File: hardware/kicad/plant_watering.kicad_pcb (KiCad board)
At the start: 2 copper layers, 143 x 112 mm, 52 parts, among them J1 USB-C panel cable (PH2.0 6P), J10 Pump2_12V, J11 Pump3_12V, J12 Pump4_12V, J13 Pump5_12V, J14 Pump6_12V, J15 Float switch (water level), J2 UI MODULE, J3 Sensor1 (GND,VCC,DIS,OUT), J4 Sensor2 (GND,VCC,DIS,OUT), J5 Sensor3 (GND,VCC,DIS,OUT), J6 Sensor4 (GND,VCC,DIS,OUT), J7 Sensor5 (GND,VCC,DIS,OUT), J8 Sensor6 (GND,VCC,DIS,OUT), J9 Pump1_12V, Q1 IRLZ44N, Q2 IRLZ44N, Q3 IRLZ44N, Q4 IRLZ44N, Q5 IRLZ44N, Q6 IRLZ44N, U1 YD-ESP32-23

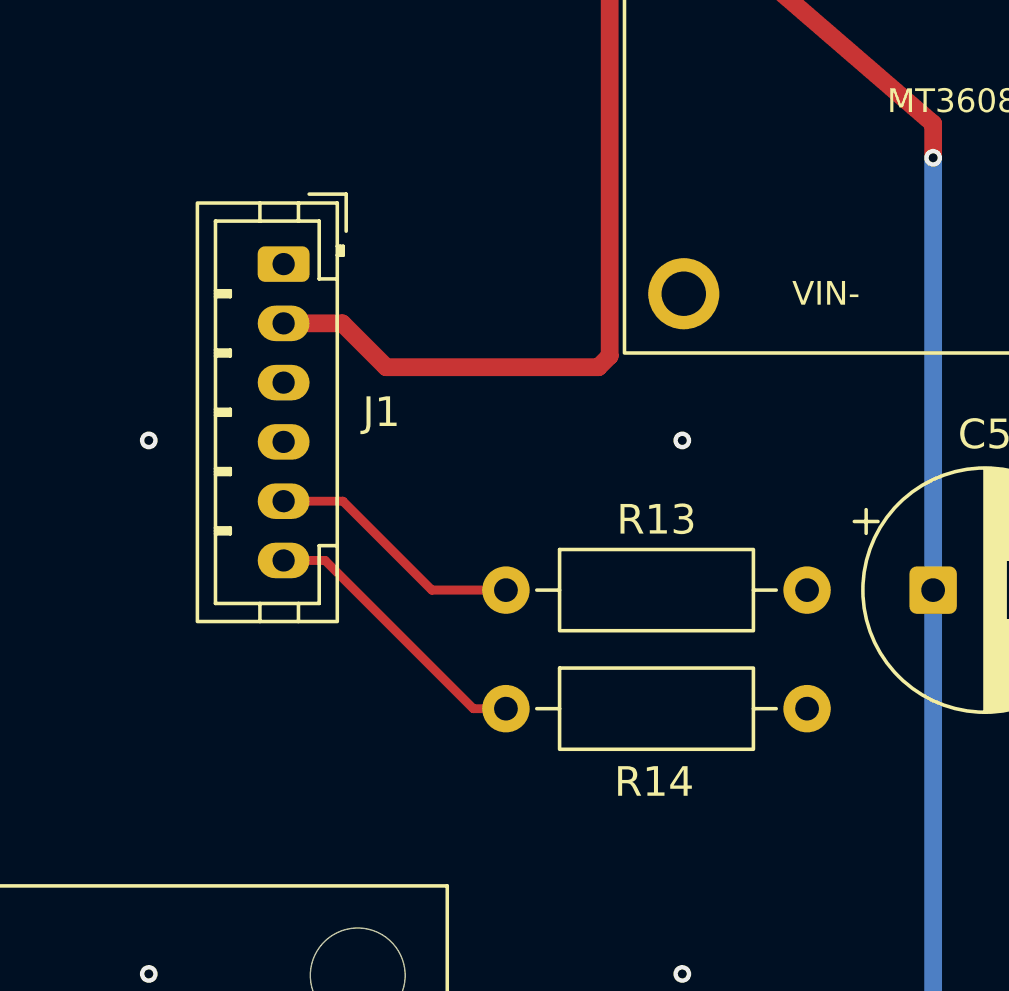
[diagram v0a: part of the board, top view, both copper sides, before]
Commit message: Simplify USB-C power input to a 2-pin V+/V- connector
J1 becomes a JST-XH 2-pin header (1 GND, 2 +5V) for a 2-wire panel
USB-C socket. Drop the CC pull-downs R13/R14 and the CC1/CC2 nets; the
socket must provide its own 5.1k CC resistors for C-to-C chargers.
Update BOM, README and the 3D view image.

Co-Authored-By: Claude Opus 5.5 <noreply@anthropic.com>
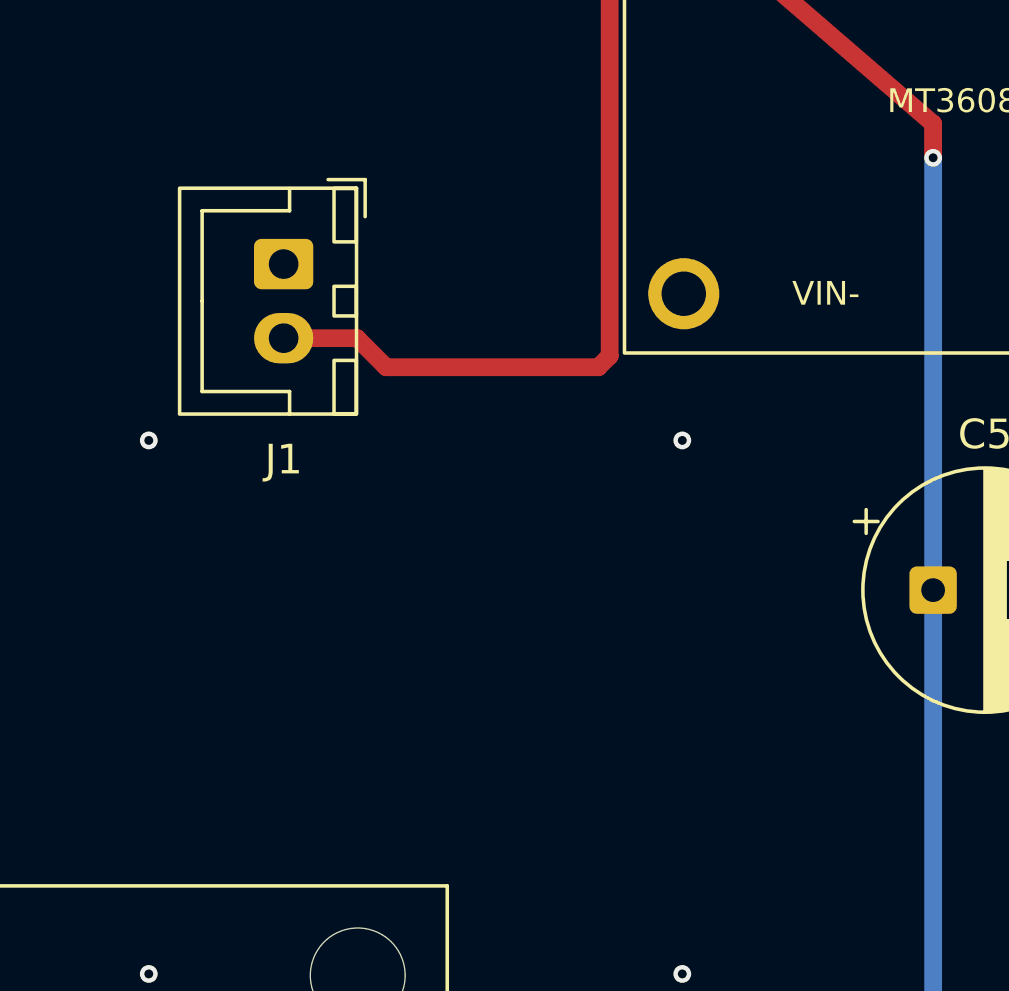
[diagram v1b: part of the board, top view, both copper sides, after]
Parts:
- removed R13, R14: 5.1k, Resistor_THT:R_Axial_DIN0207_L6.3mm_D2.5mm_P10.16mm_Horizontal
- J1: value USB-C panel cable (PH2.0 6P) -> USB-C panel socket (V+/V-); footprint Connector_JST:JST_PH_B6B-PH-K_1x06_P2.00mm_Vertical -> Connector_JST:JST_XH_B2B-XH-A_1x02_P2.50mm_Vertical
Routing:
- net CC2: track 9.57 -> 0.00 mm
- net CC1: track 8.74 -> 0.00 mm

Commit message: Add board title and goat logo to silkscreen; drop prototypy.com export
- Top-left silkscreen: goat logo (source in hardware/kicad/goat_logo.svg)
  and "Another watering system v0.1"
- export_fab.py now writes only the standard Gerber zip; removed the
  prototypy.com zip, their KiCad guide PDF and the related docs
- Regenerated plant_watering-gerbers.zip

Co-Authored-By: Claude Opus 5.5 <noreply@anthropic.com>
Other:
- board text added: "Another watering system v0.1"
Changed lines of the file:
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@@
 		)
+	)
+	(gr_poly
+		(pts
+			(xy 36.351239 55.749031) (xy 36.816115 55.842007) (xy 36.53719 56.771759) (xy 36.351239 55.749031)
+		)
+		(stroke
+			(width 0)
+			(type solid)
+		)
+		(fill yes)
+		(layer "F.SilkS")
+	)
+	(gr_poly
+		(pts
+			(xy 30.493802 56.585809) (xy 29.75 55.656056) (xy 30.028925 55.563081) (xy 30.865702 56.306883) (xy 30.493802 56.585809)
+		)
+		(stroke
+			(width 0)
+			(type solid)
+		)
+		(fill yes)
+		(layer "F.SilkS")
+	)
+	(gr_poly
+		(pts
+			(xy 34.119834 56.399858) (xy 35.328513 54.726304) (xy 36.072314 55.098205) (xy 35.142562 57.32961)
+			(xy 34.119834 56.399858)
+		)
+		(stroke
+			(width 0)
+			(type solid)
+		)
+		(fill yes)
+		(layer "F.SilkS")
+	)
+	(gr_poly
+		(pts
+			(xy 35.421487 55.00523) (xy 34.398761 55.19118) (xy 34.58471 55.470106) (xy 35.514463 55.284155)
+			(xy 35.421487 55.00523)
+		)
+		(stroke
+			(width 0)
+			(type solid)
+		)
+		(fill yes)
+		(layer "F.SilkS")
+	)
+	(gr_poly
+		(pts
+			(xy 30.772728 57.980437) (xy 31.237603 57.980437) (xy 31.144628 60.025891) (xy 31.330579 60.304817)
+			(xy 30.772728 60.304817) (xy 30.772728 60.025891) (xy 30.772728 57.980437)
+		)
+		(stroke
+			(width 0)
+			(type solid)
+		)
+		(fill yes)
+		(layer "F.SilkS")
+	)
+	(gr_poly
+		(pts
+			(xy 31.516529 57.980437) (xy 31.981405 57.980437) (xy 31.88843 60.025891) (xy 32.07438 60.304817)
+			(xy 31.516529 60.304817) (xy 31.516529 60.025891) (xy 31.516529 57.980437)
+		)
+		(stroke
+			(width 0)
+			(type solid)
+		)
+		(fill yes)
+		(layer "F.SilkS")
+	)
+	(gr_poly
+		(pts
+			(xy 33.840909 57.980437) (xy 34.305785 57.980437) (xy 34.21281 60.025891) (xy 34.398761 60.304817)
+			(xy 33.840909 60.304817) (xy 33.840909 60.025891) (xy 33.840909 57.980437)
+		)
+		(stroke
+			(width 0)
+			(type solid)
+		)
+		(fill yes)
+		(layer "F.SilkS")
+	)
+	(gr_poly
+		(pts
+			(xy 34.58471 57.887462) (xy 35.049587 57.701511) (xy 34.956612 60.025891) (xy 35.142562 60.304817)
+			(xy 34.58471 60.304817) (xy 34.58471 60.025891) (xy 34.58471 57.887462)
+		)
+		(stroke
+			(width 0)
+			(type solid)
+		)
+		(fill yes)
+		(layer "F.SilkS")
+	)
+	(gr_poly
+		(pts
+			(xy 35.607438 54.540354) (xy 35.51188 54.392497) (xy 35.411157 54.258846) (xy 35.305268 54.139399)
+			(xy 35.194215 54.034155) (xy 35.077996 53.943118) (xy 34.956612 53.866284) (xy 34.830062 53.803655)
+			(xy 34.698347 53.75523) (xy 34.561467 53.72101) (xy 34.419421 53.700995) (xy 34.27221 53.695184)
+			(xy 34.119834 53.703577) (xy 34.061725 53.719719) (xy 34.011364 53.737152) (xy 33.96875 53.755875)
+			(xy 33.933885 53.775891) (xy 33.906767 53.797198) (xy 33.887397 53.819796) (xy 33.875775 53.843686)
+			(xy 33.871901 53.868867) (xy 33.875775 53.895339) (xy 33.887397 53.923102) (xy 33.906767 53.952156)
+			(xy 33.933885 53.982503) (xy 34.070764 53.973464) (xy 34.202479 53.977337) (xy 34.329029 53.994124)
+			(xy 34.450413 54.023825) (xy 34.566632 54.066438) (xy 34.677686 54.121965) (xy 34.783575 54.190405)
+			(xy 34.884298 54.271759) (xy 34.979855 54.366026) (xy 35.070248 54.473205) (xy 35.155475 54.593298)
+			(xy 35.235537 54.726304) (xy 35.607438 54.540354)
+		)
+		(stroke
+			(width 0)
+			(type solid)
+		)
+		(fill yes)
+		(layer "F.SilkS")
+	)
+	(gr_poly
+		(pts
+			(xy 35.328513 54.633329) (xy 35.405991 54.575866) (xy 35.483471 54.52744) (xy 35.560951 54.488055)
+			(xy 35.63843 54.45771) (xy 35.715909 54.436403) (xy 35.793388 54.424135) (xy 35.870868 54.420906)
+			(xy 35.948347 54.426718) (xy 36.025827 54.441568) (xy 36.103306 54.465458) (xy 36.180785 54.498386)
+			(xy 36.258264 54.540354) (xy 37.188017 55.377131) (xy 37.215135 55.437823) (xy 37.234504 55.495933)
+			(xy 37.246126 55.55146) (xy 37.25 55.604403) (xy 37.246126 55.654765) (xy 37.234504 55.702544) (xy 37.215135 55.747741)
+			(xy 37.188017 55.790354) (xy 37.153151 55.830385) (xy 37.110537 55.867833) (xy 37.060175 55.902699)
+			(xy 37.002066 55.934982) (xy 36.351239 55.842007) (xy 36.244705 55.809078) (xy 36.142045 55.772276)
+			(xy 36.04326 55.731599) (xy 35.948347 55.687048) (xy 35.857309 55.638624) (xy 35.770145 55.586325)
+			(xy 35.686854 55.530153) (xy 35.607438 55.470106) (xy 35.531896 55.406186) (xy 35.460228 55.338391)
+			(xy 35.392433 55.266723) (xy 35.328513 55.19118) (xy 35.328513 54.633329)
+		)
+		(stroke
+			(width 0)
+			(type solid)
+		)
+		(fill yes)
+		(layer "F.SilkS")
+	)
+	(gr_poly
+		(pts
+			(xy 30.400827 56.678784) (xy 30.438275 56.590328) (xy 30.488636 56.510912) (xy 30.551911 56.440534)
+			(xy 30.628099 56.379197) (xy 30.717201 56.326899) (xy 30.819215 56.283639) (xy 30.934143 56.249419)
+			(xy 31.061984 56.224238) (xy 31.202737 56.208097) (xy 31.356405 56.200995) (xy 31.522986 56.202931)
+			(xy 31.70248 56.213907) (xy 34.119834 56.213907) (xy 34.268982 56.233923) (xy 34.406509 56.262978)
+			(xy 34.532412 56.301072) (xy 34.646694 56.348205) (xy 34.749354 56.404378) (xy 34.840393 56.469589)
+			(xy 34.919809 56.54384) (xy 34.987603 56.627131) (xy 35.043776 56.719461) (xy 35.088327 56.820829)
+			(xy 35.121255 56.931237) (xy 35.142562 57.050684) (xy 35.152247 57.201124) (xy 35.15031 57.342524)
+			(xy 35.136751 57.474884) (xy 35.11157 57.598205) (xy 35.074768 57.712487) (xy 35.026343 57.81773)
+			(xy 34.966296 57.913934) (xy 34.894628 58.001098) (xy 34.811338 58.079223) (xy 34.716425 58.148309)
+			(xy 34.609892 58.208355) (xy 34.491736 58.259362) (xy 31.144628 58.352337) (xy 31.010976 58.331677)
+			(xy 30.888946 58.300684) (xy 30.778538 58.259362) (xy 30.679752 58.20771) (xy 30.592588 58.145726)
+			(xy 30.517046 58.073412) (xy 30.453125 57.990767) (xy 30.400827 57.897792) (xy 30.36015 57.794486)
+			(xy 30.331095 57.68085) (xy 30.313662 57.556883) (xy 30.307851 57.422586) (xy 30.400827 56.678784)
+		)
+		(stroke
+			(width 0)
+			(type solid)
+		)
+		(fill yes)
+		(layer "F.SilkS")
 	)
 	(gr_arc
@@
 		(layer "Edge.Cuts")
 	)
+	(gr_text "Another watering system v0.1"
+		(at 36 62 0)
+		(layer "F.SilkS")
+		(effects
+			(font
+				(size 1.5 1.5)
+				(thickness 0.25)
+			)
+		)
+	)
 	(segment
 		(start 121.66 42)
@@
 	)
 	(segment
+		(start 49.98 47.5)
+		(end 50.96 48.48)
+		(width 0.6)
+		(layer "F.Cu")
+		(net "+5V")
+	)
+	(segment
+		(start 58.5 35.5)
+		(end 61 33)
+		(width 0.6)
+		(layer "F.Cu")
+		(net "+5V")
+	)
+	(segment
+		(start 58.1183 48.48)
+		(end 58.5 48.0983)
+		(width 0.6)
+		(layer "F.Cu")
+		(net "+5V")
+	)
+	(segment
+		(start 58.5 48.0983)
+		(end 58.5 35.5)
+		(width 0.6)
+		(layer "F.Cu")
+		(net "+5V")
+	)
+	(segment
+		(start 61 33)
+		(end 69.4133 40.2633)
+		(width 0.6)
+		(layer "F.Cu")
+		(net "+5V")
+	)
+	(segment
+		(start 47.5 47.5)
+		(end 49.98 47.5)
+		(width 0.6)
+		(layer "F.Cu")
+		(net "+5V")
+	)
+	(segment
+		(start 69.4133 40.2633)
+		(end 69.4133 41.4133)
+		(width 0.6)
+		(layer "F.Cu")
+		(net "+5V")
+	)
+	(segment
+		(start 50.96 48.48)
+		(end 58.1183 48.48)
+		(width 0.6)
+		(layer "F.Cu")
+		(net "+5V")
+	)
+	(via
+		(at 69.4133 41.4133)
+		(size 0.6)
+		(drill 0.3)
+		(layers "F.Cu" "B.Cu")
+		(net "+5V")
+	)
+	(segment
+		(start 69.4133 119.3867)
+		(end 62 126.8)
+		(width 0.6)
+		(layer "B.Cu")
+		(net "+5V")
+	)
+	(segment
+		(start 69.4133 41.4133)
+		(end 69.4133 119.3867)
+		(width 0.6)
+		(layer "B.Cu")
+		(net "+5V")
+	)
+	(segment
 		(start 148.5 91)
 		(end 143.16 91)
@@
 	)
 	(segment
-		(start 49.98 47.5)
-		(end 50.96 48.48)
-		(width 0.6)
-		(layer "F.Cu")
-		(net "+5V")
-	)
-	(segment
-		(start 58.5 35.5)
-		(end 61 33)
-		(width 0.6)
-		(layer "F.Cu")
-		(net "+5V")
-	)
-	(segment
-		(start 58.1183 48.48)
-		(end 58.5 48.0983)
-		(width 0.6)
-		(layer "F.Cu")
-		(net "+5V")
-	)
-	(segment
-		(start 58.5 48.0983)
-		(end 58.5 35.5)
-		(width 0.6)
-		(layer "F.Cu")
-		(net "+5V")
-	)
-	(segment
-		(start 61 33)
-		(end 69.4133 40.2633)
-		(width 0.6)
-		(layer "F.Cu")
-		(net "+5V")
-	)
-	(segment
-		(start 47.5 47.5)
-		(end 49.98 47.5)
-		(width 0.6)
-		(layer "F.Cu")
-		(net "+5V")
-	)
-	(segment
-		(start 69.4133 40.2633)
-		(end 69.4133 41.4133)
-		(width 0.6)
-		(layer "F.Cu")
-		(net "+5V")
-	)
-	(segment
-		(start 50.96 48.48)
-		(end 58.1183 48.48)
-		(width 0.6)
-		(layer "F.Cu")
-		(net "+5V")
-	)
-	(via
-		(at 69.4133 41.4133)
-		(size 0.6)
-		(drill 0.3)
-		(layers "F.Cu" "B.Cu")
-		(net "+5V")
-	)
-	(segment
-		(start 69.4133 119.3867)
-		(end 62 126.8)
-		(width 0.6)
-		(layer "B.Cu")
-		(net "+5V")
-	)
-	(segment
-		(start 69.4133 41.4133)
-		(end 69.4133 119.3867)
-		(width 0.6)
-		(layer "B.Cu")
-		(net "+5V")
-	)
-	(segment
